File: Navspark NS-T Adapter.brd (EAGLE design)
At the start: 74.9 x 54.6 mm, 5 parts

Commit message: remove PLL OE -> GND, rely on internal pullup
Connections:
- net GND: no longer U$2.7
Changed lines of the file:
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@@
 <contactref element="U$4" pad="1"/>
 <contactref element="U$4" pad="7"/>
-<contactref element="U$2" pad="7"/>
 </signal>
 <signal name="N$3">

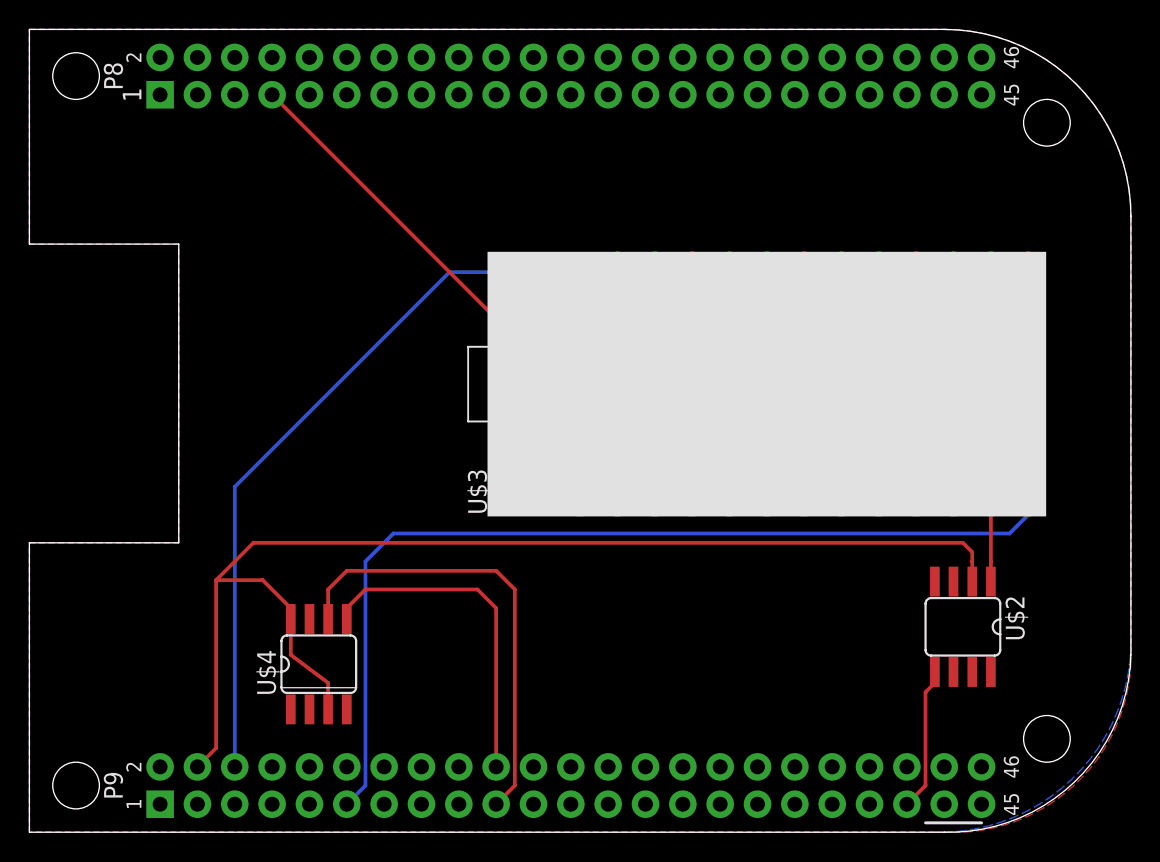
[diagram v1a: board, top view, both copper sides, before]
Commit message: revision 2: decouple NS-T/PI6C4511, add limiting resistor between PI6C4511 and BBB
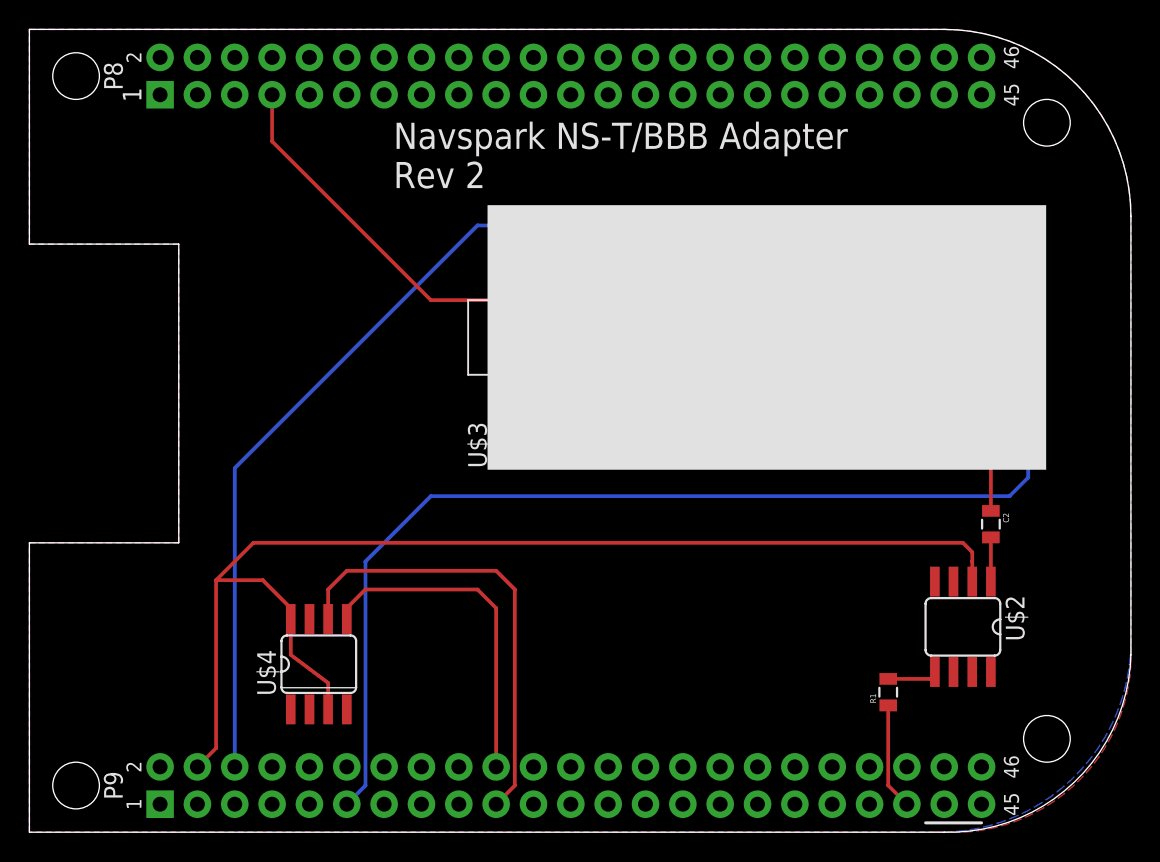
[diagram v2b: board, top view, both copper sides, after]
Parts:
- added C2: 10nF, SparkFun-Capacitors:0805
- added R1: 270, SparkFun-Resistors:0805
- moved U$3 3.17 mm to (56.5, 43.8)
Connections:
- new net N$10: R1.2, U$2.5
- new net N$9: C2.2, U$2.1
- net N$5: now also R1.1; no longer U$2.5
- net N$6: now also C2.1; no longer U$2.1
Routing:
- net N$10: track 0.00 -> 4.02 mm
- net N$9: track 0.00 -> 3.01 mm
- net N$5: track 9.78 -> 7.25 mm
- net +5V: track 51.1 -> 53.2 mm
- net N$4: track 64.7 -> 66.4 mm
- net N$6: track 5.82 -> 4.18 mm
- net N$3: track 42.5 -> 43.8 mm
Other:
- board text added: "Daniel Drown (based on a design by) Casey Kuhns"
- board text added: "Navspark NS-T/BBB Adapter Rev 2"
- board text removed: "Casey Kuhns"
